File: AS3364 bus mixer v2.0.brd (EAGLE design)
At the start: 44.5 x 33 mm, 73 parts, among them IC1 TL072JT, IC2 TL072JT, IC3 TL072JT, IC30 TL072JT, IC4 TL072JT, IC5 79L09F, IC6 78L09F, IC7 CH446Q

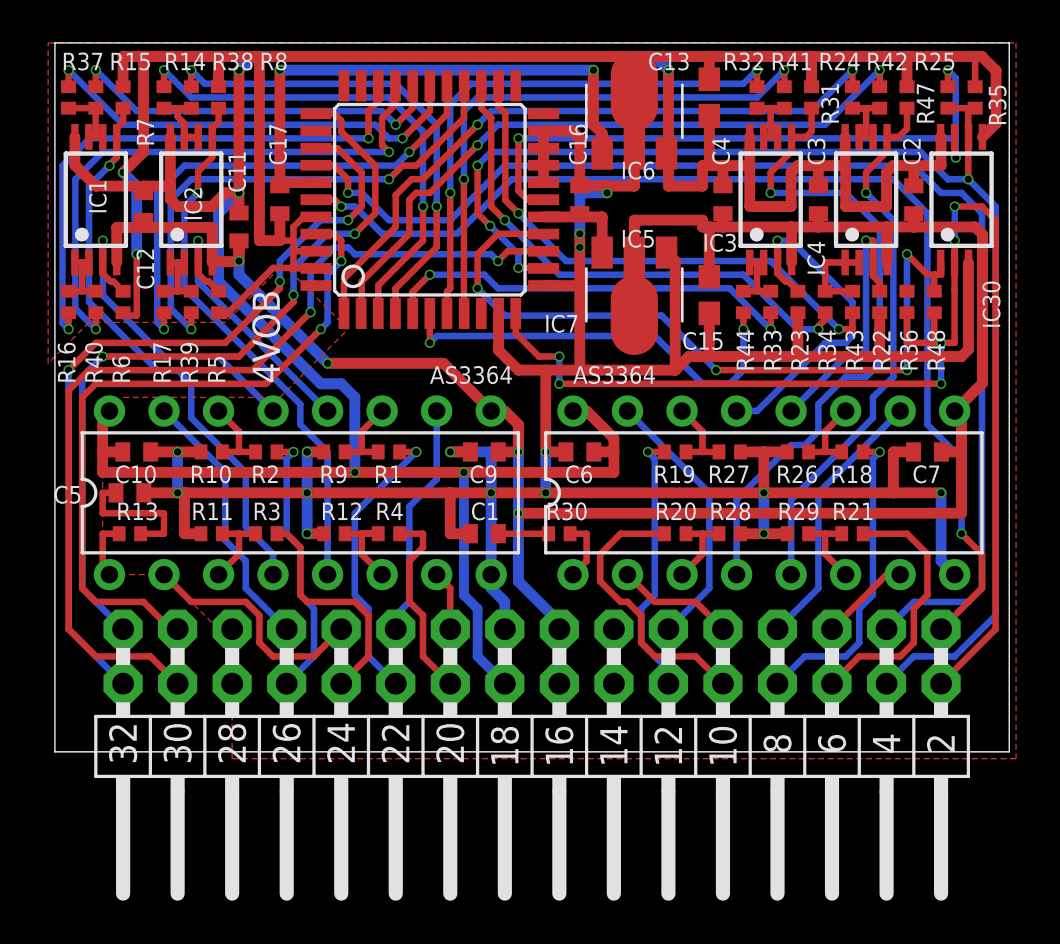
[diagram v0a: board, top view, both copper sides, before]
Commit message: Ordered 10 bus mixer v2.0
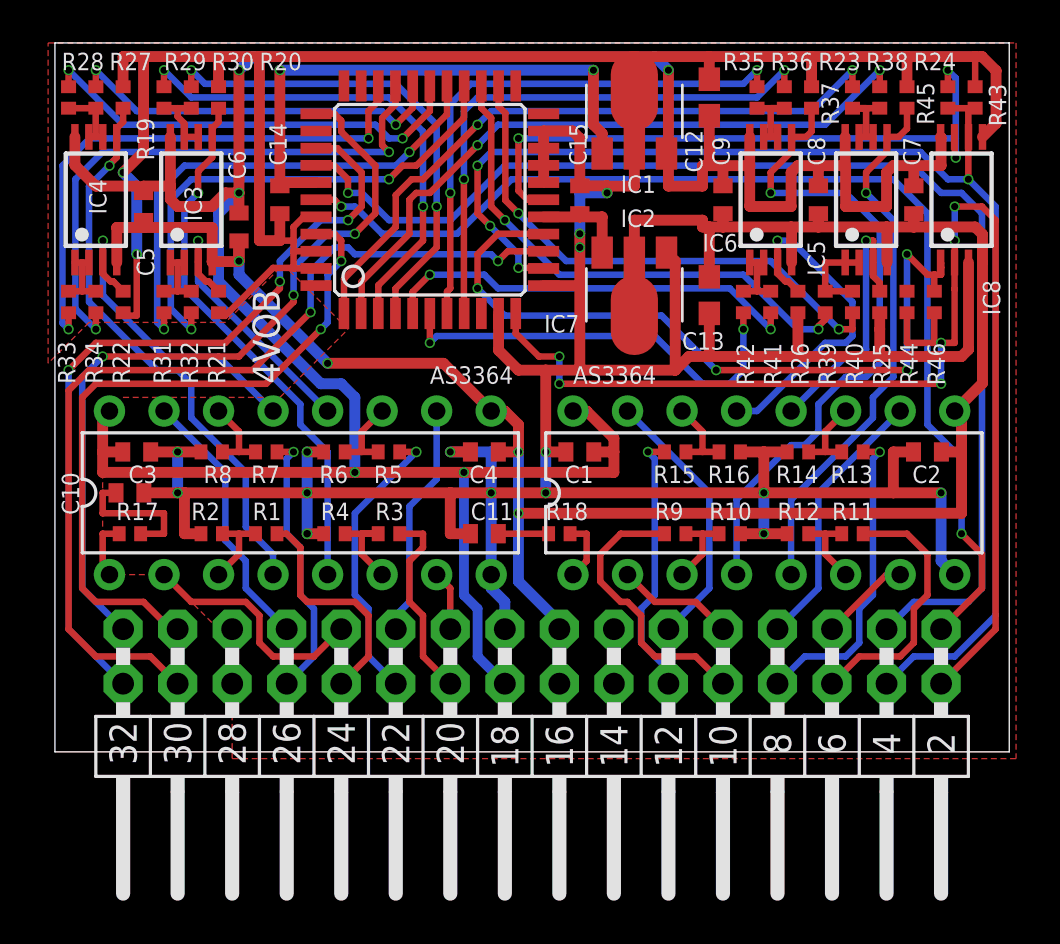
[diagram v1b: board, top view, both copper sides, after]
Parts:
- removed C16: 100nF, rcl:C0402
- added C8: 100nF, rcl:C0402
- C1, C5: value 5nF -> 100nF
- C10, C11: value 100nF -> 5nF
- C12: value 100nF -> 0.33uF; device rcl:C0402 -> resistor:C0603
- C15: value 0.33uF -> 100nF; device resistor:C0603 -> rcl:C0402
- IC1: value TL072JT -> 78L09F; device joakim:TSSOP8J -> linear:SOT89
- IC2: value TL072JT -> 79L09F; device joakim:TSSOP8J -> joakim:SOT89
- IC5: value 79L09F -> TL072JT; device joakim:SOT89 -> joakim:TSSOP8J
- IC6: value 78L09F -> TL072JT; device linear:SOT89 -> joakim:TSSOP8J
- R11, R26, R27, R28, R29, R9: value 22k -> 33k
- R13, R30: value 100R -> 33k
- R14, R16, R6, R8: value 36k -> 22k
- R15, R22, R23, R24, R25, R31, R32, R33, R34, R37, R38, R39, R40, R41, R42, R5, R7: value 36k -> 33k
- R17: value 36k -> 100R
- R18: value 33k -> 100R
- R2, R4: value 33k -> 22k
- R35, R36: value 220k -> 33k
- R43, R44: value 36k -> 220k
- moved R28 36.9 mm to (0.64, 30.8), turned to 90 degrees
- moved R37 36.5 mm to (37.1, 30.8)
- moved IC4 35.9 mm to (1.91, 26.0)
- moved R29 35.8 mm to (5.08, 30.8), turned to 90 degrees
- moved R22 35.2 mm to (3.17, 21.3)
- moved R40 35.2 mm to (37.1, 21.3)
- moved R34 34.0 mm to (1.91, 21.3)
- moved R13 33.9 mm to (37.1, 14.3)
- moved C3 33.9 mm to (3.81, 14.3), turned to 180 degrees
- moved R14 33.8 mm to (34.6, 14.3), turned to 0 degrees
- moved R27 33.8 mm to (1.91, 30.8), turned to 90 degrees
- moved R31 33.5 mm to (5.08, 21.3), turned to 270 degrees
- moved R33 32.7 mm to (0.64, 21.3)
- moved R38 32.1 mm to (38.4, 30.8)
- moved R15 31.6 mm to (28.9, 14.3), turned to 0 degrees
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- renumbered C17 to C14, DA1 to IC10, DA2 to IC9, IC30 to IC8, R47 to R45, R48 to R46, SV1 to X1
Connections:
- net +12V: now also C1.2, C5.2, C7.2, C8.2, C9.2, IC1.3, IC5.8, IC6.8; no longer C10.2, C11.2, C13.2, C2.2, C4.2, IC1.8, IC2.8, IC6.3
- net +9V: now also IC1.1; no longer IC6.1
- net -12V: now also C13.1, C5.1, C6.1, C8.1, IC2.2, IC2.2@1, IC5.4, IC6.4; no longer C11.1, C12.1, C15.1, C3.1, IC1.4, IC2.4, IC5.2, IC5.2@1
- net -9V: now also C15.2, IC2.3; no longer C16.2, IC5.3
- net BUS_A: now also R43.2; no longer R35.2
- net BUS_B: now also R44.2; no longer R36.2
- net CON1: now also IC4.3, R22.2; no longer IC1.3, R6.2
- net CON2: now also IC4.5, R19.2; no longer IC1.5, R7.2
- net CON3: now also IC3.3, R21.2; no longer IC2.3, R5.2
- net CON4: now also IC3.5, R20.2; no longer IC2.5, R8.2
- net CON5: now also IC6.3, R26.2; no longer IC3.3, R23.2
- net CON6: now also IC6.5, R23.2; no longer IC3.5, R24.2
- net CON7: now also IC5.3, R25.2; no longer IC4.3, R22.2
- net CON8: now also IC5.5, R24.2; no longer IC4.5, R25.2
- net CV1: now also R7.1; no longer R2.1
- net CV2: now also R1.1; no longer R3.1
- net CV2_IN: now also R1.2, R2.2; no longer R11.2, R3.2
- net CV3: now also R5.1; no longer R1.1
- net CV4: now also R3.1; no longer R4.1
- net CV5: now also R15.1; no longer R19.1
- net CV6: now also R9.1; no longer R20.1
- net CV6_IN: now also R10.2, R9.2; no longer R20.2, R28.2
- net CV7: now also R13.1; no longer R18.1
- net CV8: now also R11.1; no longer R21.1
- net GND: now also C11.1, C12.1, C13.2, C15.1, C2.2, C3.1, C4.2, IC1.2, IC1.2@1, IC2.1, R14.1, R16.1, R19.1, R2.1, R20.1, R21.1, R4.1, R43.1, R44.1; no longer C13.1, C15.2, C16.1, C5.1, C6.1, C7.2, C9.2, IC5.1, IC6.2, IC6.2@1, R11.1, R27.1, R28.1, R29.1, R35.1, R36.1, R5.1, R7.1, R9.1
- net N$1: now also R18.2; no longer R30.2
- net N$10: now also R3.2; no longer R12.2
- net N$12: now also R5.2, R6.2; no longer R1.2, R9.2
- net N$14: now also C10.2, R17.1; no longer C5.2, R13.1
- net N$2: now also R17.2; no longer R13.2
- net N$21: now also R7.2, R8.2; no longer R10.2, R2.2
- net N$3: now also R11.2, R12.2; no longer R21.2, R29.2
- net N$5: now also R13.2, R14.2; no longer R18.2, R26.2
- net N$7: now also R15.2, R16.2; no longer R19.2, R27.2
- net N$8: now also C11.2, R18.1; no longer C1.2, R30.1
- net OUT1: now also IC4.1, IC4.2, R33.1, R34.1; no longer IC1.1, IC1.2, R16.1, R40.1
- net OUT2: now also IC4.6, IC4.7, R27.1, R28.1; no longer IC1.6, IC1.7, R15.1, R37.1
- net OUT3: now also IC3.1, IC3.2, R31.1, R32.1; no longer IC2.1, IC2.2, R17.1, R39.1
- net OUT4: now also IC3.6, IC3.7, R29.1, R30.1; no longer IC2.6, IC2.7, R14.1, R38.1
- net OUT5: now also IC6.1, IC6.2, R41.1, R42.1; no longer IC3.1, IC3.2, R33.1, R44.1
- net OUT6: now also IC6.6, IC6.7, R35.1, R36.1; no longer IC3.6, IC3.7, R32.1, R41.1
- net OUT7: now also IC5.1, IC5.2, R39.1, R40.1; no longer IC4.1, IC4.2, R34.1, R43.1
- net OUT8: now also IC5.6, IC5.7, R37.1, R38.1; no longer IC4.6, IC4.7, R31.1, R42.1
- net SW1A: now also R33.2; no longer R16.2
- net SW1B: now also R34.2; no longer R40.2
- net SW2A: now also R27.2; no longer R15.2
- net SW2B: now also R28.2; no longer R37.2
- net SW3A: now also R31.2; no longer R17.2
- net SW3B: now also R32.2; no longer R39.2
- net SW4A: now also R29.2; no longer R14.2
- net SW4B: now also R30.2; no longer R38.2
- net SW5A: now also R41.2; no longer R33.2
- net SW5B: now also R42.2; no longer R44.2
- net SW6A: now also R35.2; no longer R32.2
- net SW6B: now also R36.2; no longer R41.2
- net SW7A: now also R39.2; no longer R34.2
- net SW7B: now also R40.2; no longer R43.2
- net SW8A: now also R37.2; no longer R31.2
- net SW8B: now also R38.2; no longer R42.2
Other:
- board text removed: "BC"
- board text removed: "DS"
